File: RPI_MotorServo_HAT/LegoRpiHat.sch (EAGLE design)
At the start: 11 parts, among them IC2 LM2576S, U1 A4950ELJTR-T, U2 A4950ELJTR-T, X1 RASPI_BOARD_B+_H

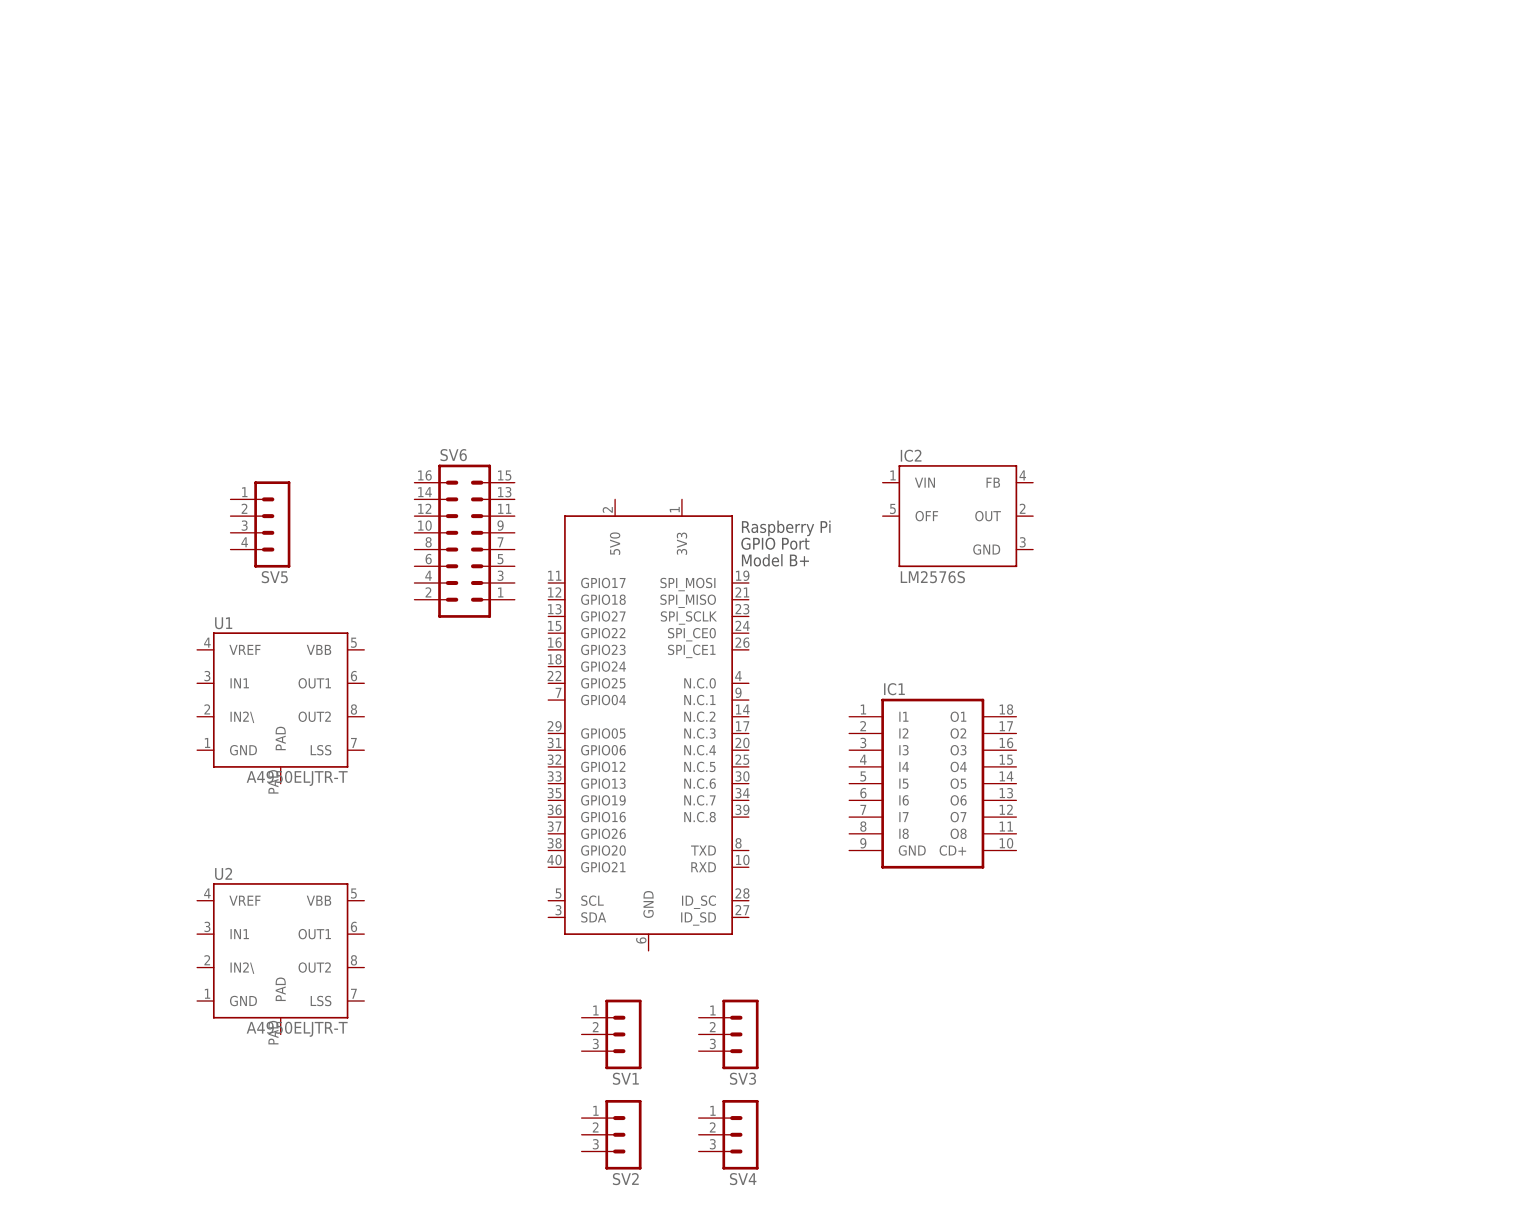
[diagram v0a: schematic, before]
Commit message: Started to make the connections. Still no passive components added
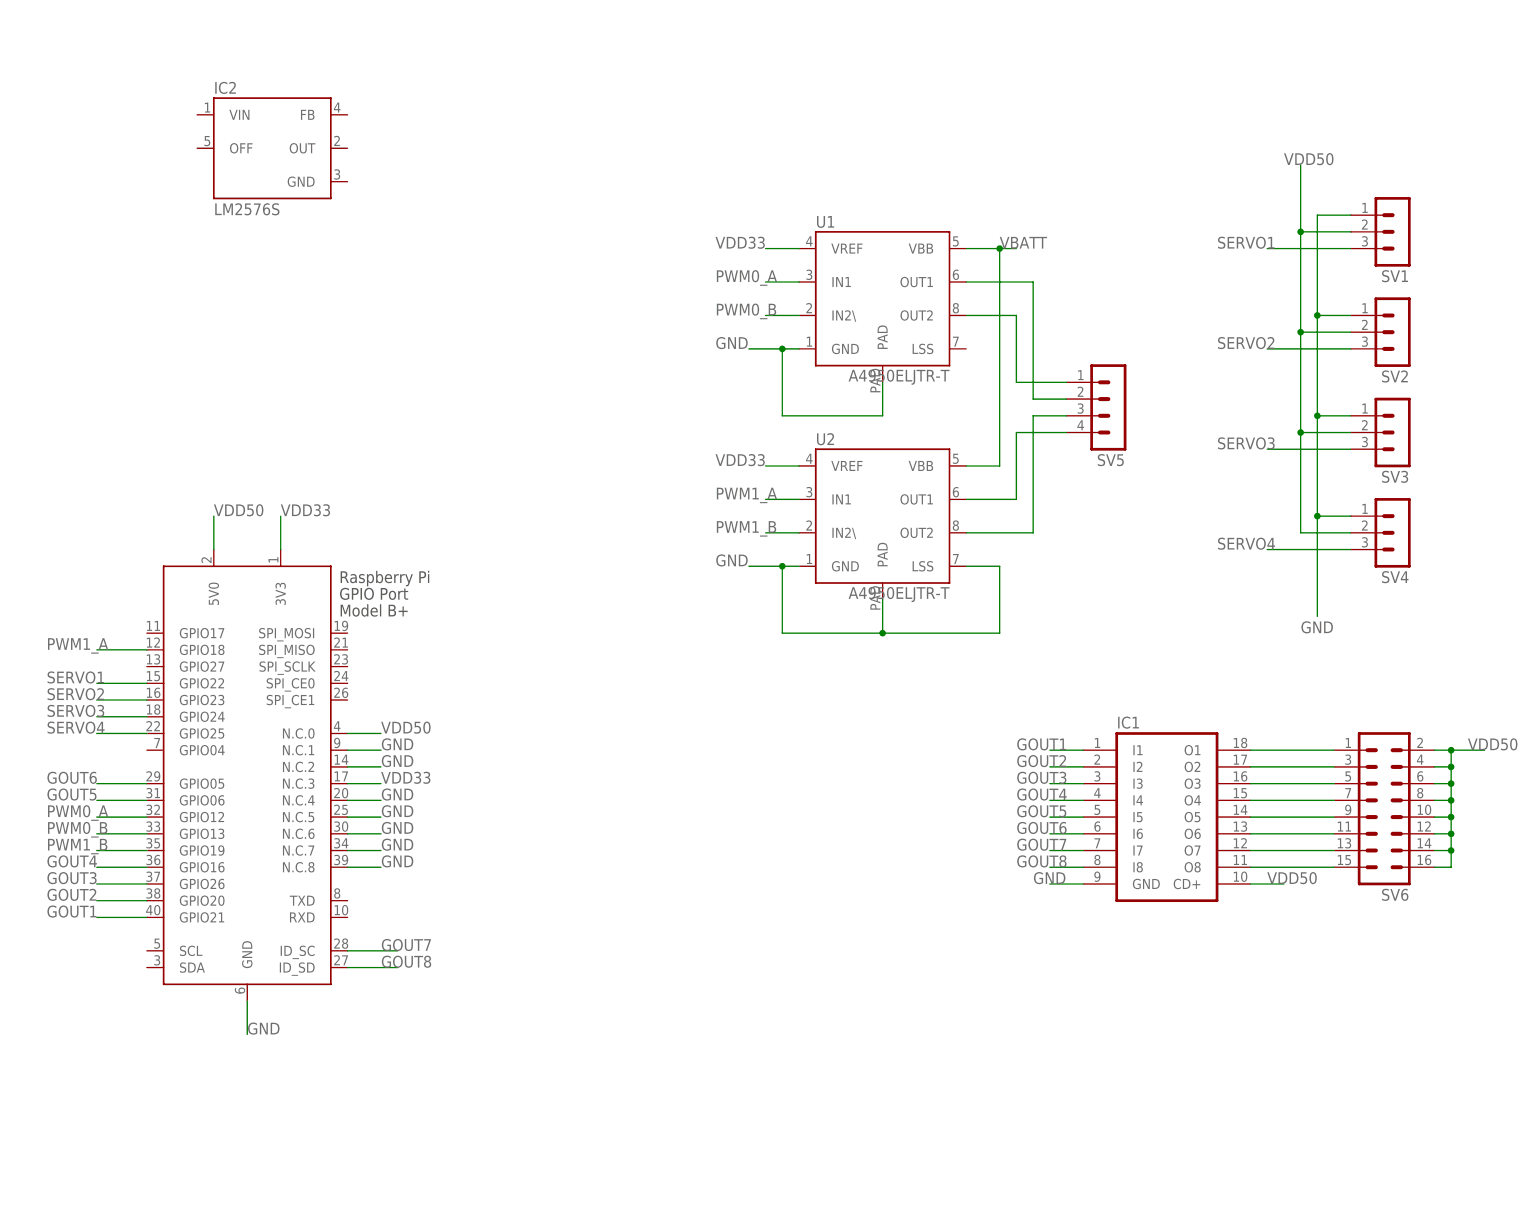
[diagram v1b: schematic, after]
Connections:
- new net GND: IC1.GND, SV1.1, SV2.1, SV3.1, SV4.1, U1.GND, U1.PAD, U2.GND, U2.LSS, U2.PAD, X1.GND, X1.N.C.1, X1.N.C.2, X1.N.C.4, X1.N.C.5, X1.N.C.6, X1.N.C.7, X1.N.C.8
- new net GOUT1: IC1.I1, X1.GPIO21
- new net GOUT2: IC1.I2, X1.GPIO20
- new net GOUT3: IC1.I3, X1.GPIO26
- new net GOUT4: IC1.I4, X1.GPIO16
- new net GOUT5: IC1.I5, X1.GPIO06
- new net GOUT6: IC1.I6, X1.GPIO05
- new net GOUT7: IC1.I7, X1.ID_SC
- new net GOUT8: IC1.I8, X1.ID_SD
- new net N$1: IC1.O1, SV6.1
- new net N$10: SV5.1, U1.OUT2
- new net N$11: SV5.4, U2.OUT1
- new net N$12: SV5.3, U2.OUT2
- new net N$2: IC1.O2, SV6.3
- new net N$3: IC1.O3, SV6.5
- new net N$4: IC1.O4, SV6.7
- new net N$5: IC1.O5, SV6.9
- new net N$6: IC1.O6, SV6.11
- new net N$7: IC1.O7, SV6.13
- new net N$8: IC1.O8, SV6.15
- new net N$9: SV5.2, U1.OUT1
- new net PWM0_A: U1.IN1, X1.GPIO12
- new net PWM0_B: U1.IN2\, X1.GPIO13
- new net PWM1_A: U2.IN1, X1.GPIO18
- new net PWM1_B: U2.IN2\, X1.GPIO19
- new net SERVO1: SV1.3, X1.GPIO22
- new net SERVO2: SV2.3, X1.GPIO23
- new net SERVO3: SV3.3, X1.GPIO24
- new net SERVO4: SV4.3, X1.GPIO25
- new net VBATT: U1.VBB, U2.VBB
- new net VDD33: U1.VREF, U2.VREF, X1.3V3, X1.N.C.3
- new net VDD50: IC1.CD+, SV1.2, SV2.2, SV3.2, SV4.2, SV6.10, SV6.12, SV6.14, SV6.16, SV6.2, SV6.4, SV6.6, SV6.8, X1.5V0, X1.N.C.0
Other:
- moved on the sheet: IC1, IC2, SV1, SV2, SV3, SV4, SV5, SV6, U1, U2

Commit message: mostly done with the schematics and the component placements. Only missing a couple of components on the 5V regulator
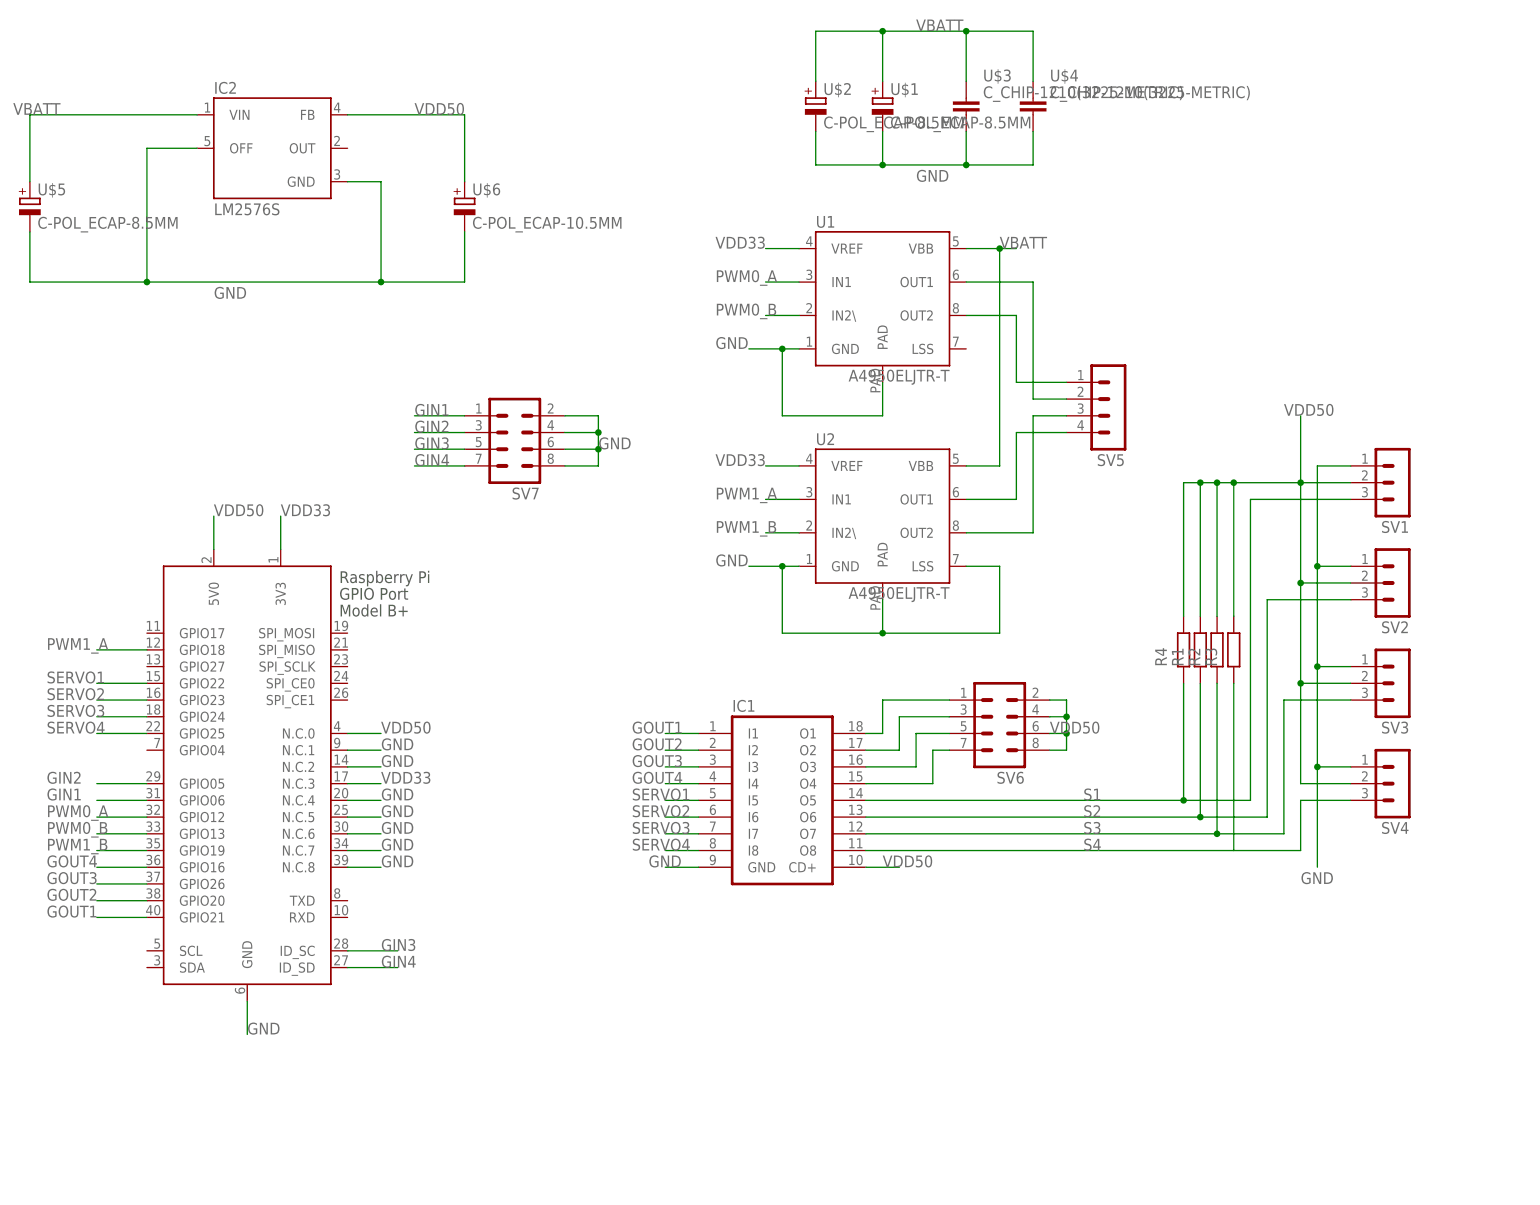
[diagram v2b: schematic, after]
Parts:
- added R1, R2, R3, R4: (no value), Resistor:R_CHIP-1206(3216-METRIC)
- added SV7: (no value), con-lstb:MA04-2
- added U$1, U$2, U$5: C-POL_ECAP-8.5MM, Capacitor:C-POL_ECAP-8.5MM
- added U$3, U$4: C_CHIP-1210(3225-METRIC), Capacitor:C_CHIP-1210(3225-METRIC)
- added U$6: C-POL_ECAP-10.5MM, Capacitor:C-POL_ECAP-10.5MM
- SV6: device con-lstb:MA08-2 -> con-lstb:MA04-2
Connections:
- removed net GOUT5: IC1.I5, X1.GPIO06
- removed net GOUT6: IC1.I6, X1.GPIO05
- removed net GOUT7: IC1.I7, X1.ID_SC
- removed net GOUT8: IC1.I8, X1.ID_SD
- removed net N$5: IC1.O5, SV6.9
- removed net N$6: IC1.O6, SV6.11
- removed net N$7: IC1.O7, SV6.13
- removed net N$8: IC1.O8, SV6.15
- new net GIN1: SV7.1, X1.GPIO06
- new net GIN2: SV7.3, X1.GPIO05
- new net GIN3: SV7.5, X1.ID_SC
- new net GIN4: SV7.7, X1.ID_SD
- new net S1: IC1.O5, R4.1, SV1.3
- new net S2: IC1.O6, R1.1, SV2.3
- new net S3: IC1.O7, R2.1, SV3.3
- new net S4: IC1.O8, R3.1, SV4.3
- net GND: now also IC2.GND, IC2.OFF, SV7.2, SV7.4, SV7.6, SV7.8, U$1.-, U$2.-, U$3.2, U$4.2, U$5.-, U$6.-
- net SERVO1: now also IC1.I5; no longer SV1.3
- net SERVO2: now also IC1.I6; no longer SV2.3
- net SERVO3: now also IC1.I7; no longer SV3.3
- net SERVO4: now also IC1.I8; no longer SV4.3
- net VBATT: now also IC2.VIN, U$1.+, U$2.+, U$3.1, U$4.1, U$5.+
- net VDD50: now also IC2.FB, R1.2, R2.2, R3.2, R4.2, U$6.+; no longer SV6.10, SV6.12, SV6.14, SV6.16
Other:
- moved on the sheet: IC1, SV1, SV2, SV3, SV4

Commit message: Testing how to generate pcb mill output
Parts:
- removed IC1: (no value), uln-udn_mod:ULN2803ASO18W
- removed R1, R2, R3, R4: (no value), Resistor:R_CHIP-1206(3216-METRIC)
- removed SV7: (no value), con-lstb:MA04-2
- added D1: MBRS340T3, diode:MBRS340T3
- added JP1: (no value), pinhead:PINHD-1X2
- added L1: DR127, inductors:DR127
- SV6: device con-lstb:MA04-2 -> con-lstb:MA06-1
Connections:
- removed net GIN1: SV7.1, X1.GPIO06
- removed net GIN2: SV7.3, X1.GPIO05
- removed net GIN3: SV7.5, X1.ID_SC
- removed net GIN4: SV7.7, X1.ID_SD
- removed net GOUT1: IC1.I1, X1.GPIO21
- removed net GOUT2: IC1.I2, X1.GPIO20
- removed net GOUT3: IC1.I3, X1.GPIO26
- removed net GOUT4: IC1.I4, X1.GPIO16
- removed net N$1: IC1.O4, SV6.7
- removed net N$2: IC1.O3, SV6.5
- removed net N$3: IC1.O2, SV6.3
- removed net N$4: IC1.O1, SV6.1
- removed net S1: IC1.O5, R4.1, SV1.3
- removed net S2: IC1.O6, R1.1, SV2.3
- removed net S3: IC1.O7, R2.1, SV3.3
- removed net S4: IC1.O8, R3.1, SV4.3
- new net N$5: D1.C, IC2.OUT, L1.1
- new net SCL: SV6.1, X1.SCL
- new net SDA: SV6.2, X1.SDA
- net GND: now also D1.A, JP1.1, SV6.3, U1.LSS; no longer IC1.GND, SV7.2, SV7.4, SV7.6, SV7.8
- net SERVO1: now also SV1.3, X1.GPIO21; no longer IC1.I5, X1.GPIO22
- net SERVO2: now also SV2.3, X1.GPIO20; no longer IC1.I6, X1.GPIO23
- net SERVO3: now also SV3.3, X1.GPIO26; no longer IC1.I7, X1.GPIO24
- net SERVO4: now also SV4.3, X1.GPIO16; no longer IC1.I8, X1.GPIO25
- net VBATT: now also JP1.2, SV6.6
- net VDD33: now also SV6.4; no longer U1.VREF, U2.VREF
- net VDD50: now also L1.2, SV6.5, U1.VREF, U2.VREF; no longer IC1.CD+, R1.2, R2.2, R3.2, R4.2, SV6.2, SV6.4, SV6.6, SV6.8
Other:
- moved on the sheet: U$6
